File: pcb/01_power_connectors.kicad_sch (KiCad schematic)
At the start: 2 parts, among them J1 XT60PW-F, J2 XT60PW-M

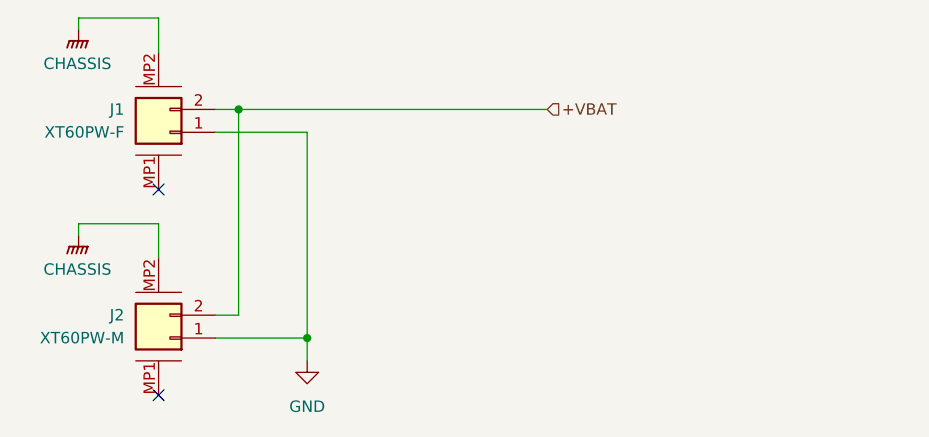
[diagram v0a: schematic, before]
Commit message: Added two XT-60 power connectors for daisy chaining multiple nodes together
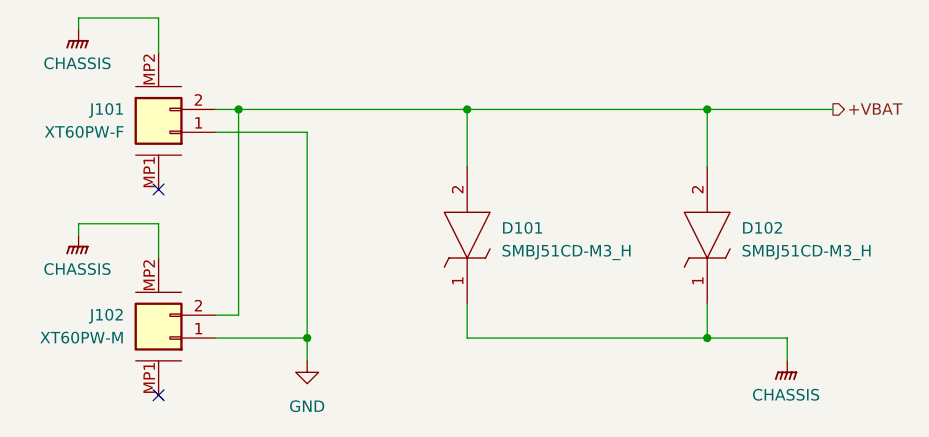
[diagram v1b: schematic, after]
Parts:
- added D101, D102: SMBJ51CD-M3_H, FluxNode-FOC:DIOM4336X24N, symbol FluxNode-FOC:SMBJ51CD-M3_H
- renumbered J1 to J101, J2 to J102
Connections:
- net +VBAT: now also D101.2, D102.2
- net CHASSIS: now also D101.1, D102.1

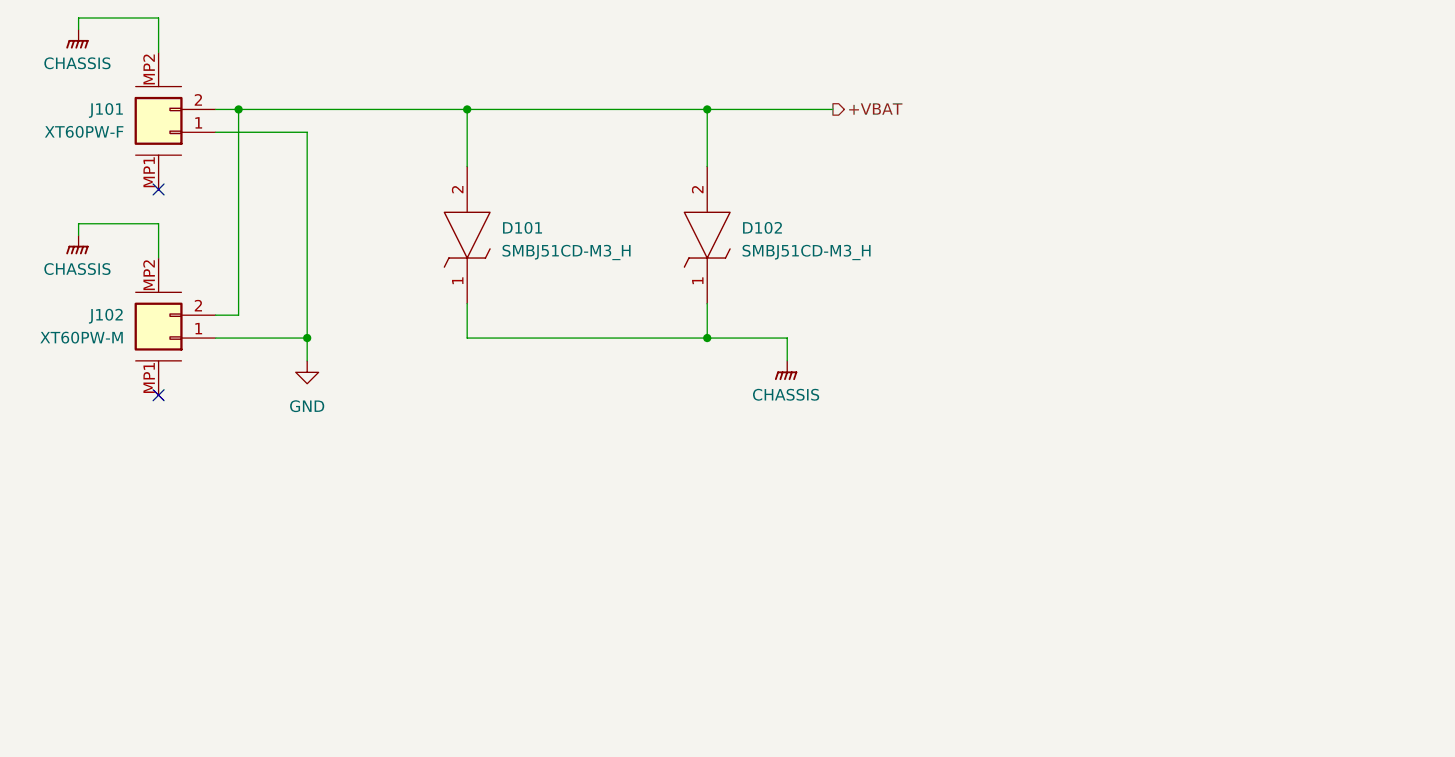
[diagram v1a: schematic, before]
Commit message: Unified all different LCSC part numbers of the same exact components to just one variant
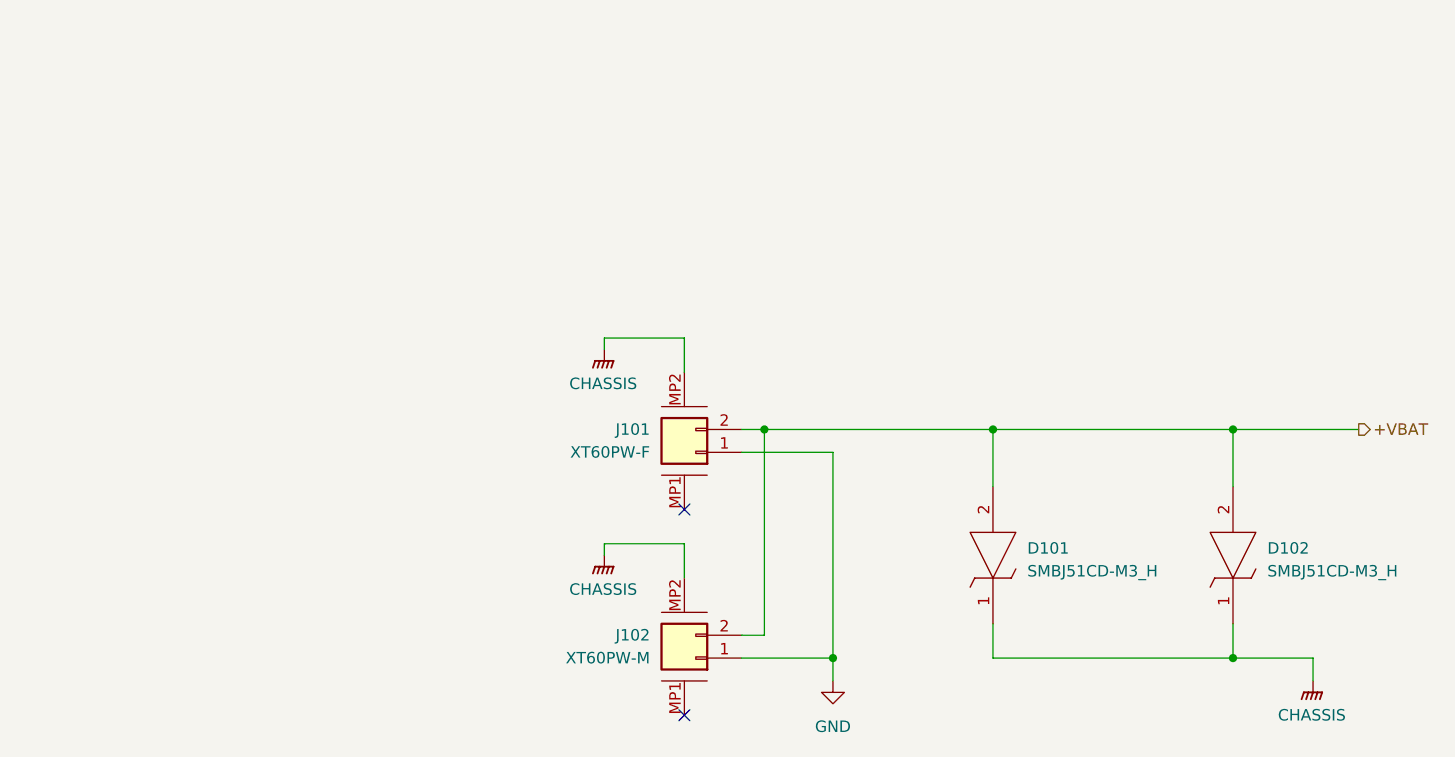
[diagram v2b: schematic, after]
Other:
- company: (none) -> PhiMai
- moved on the sheet: D101, D102, J101, J102

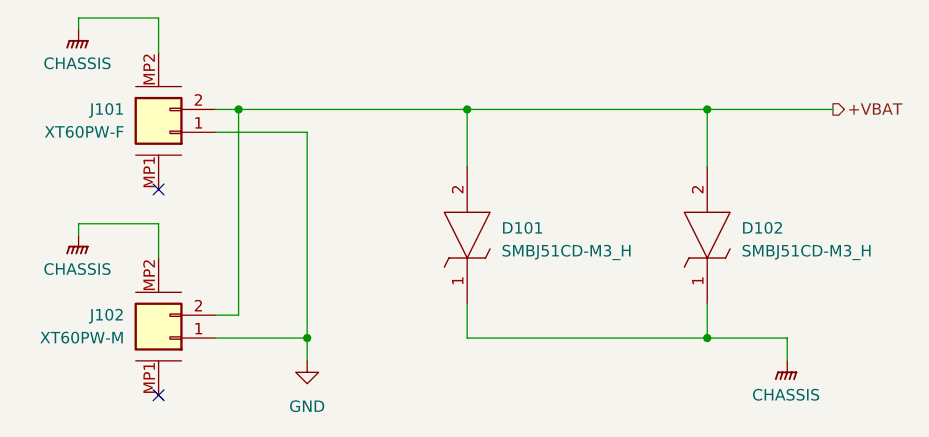
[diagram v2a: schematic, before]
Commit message: Some minor changes to the annotations
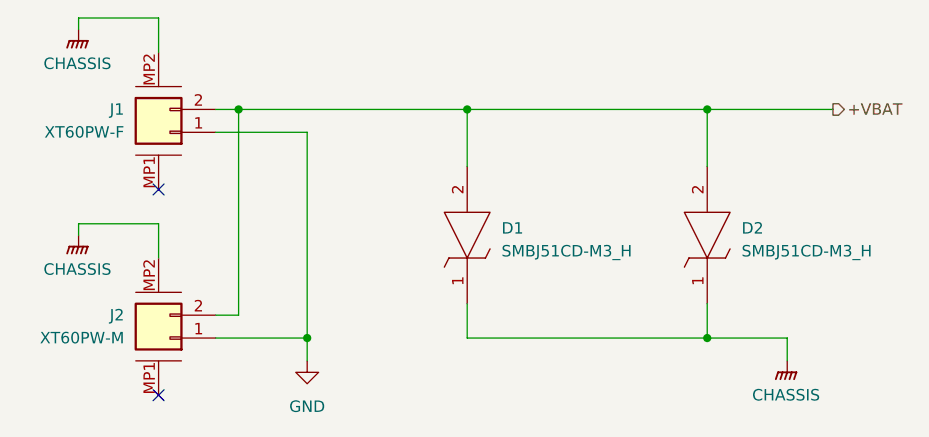
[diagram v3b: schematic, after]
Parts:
- renumbered D101 to D1, D102 to D2, J101 to J1, J102 to J2
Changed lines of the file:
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@@
 		(dnp no)
 		(fields_autoplaced yes)
-		(property "Reference" "#PWR0104"
+		(property "Reference" "#PWR09"
 			(at 179.07 107.95 0)
 			(hide yes)
@@
 			(project "FluxNode-FOC"
 				(path "/c3755418-04f3-4b36-86ed-bd05a53b8f5f/7c307646-0ecd-4068-a7a2-01ba516b03a7"
-					(reference "#PWR0104")
+					(reference "#PWR09")
 					(unit 1)
 				)
@@
 		(dnp no)
 		(fields_autoplaced yes)
-		(property "Reference" "#PWR0103"
+		(property "Reference" "#PWR08"
 			(at 125.73 109.22 0)
 			(hide yes)
@@
 			(project "FluxNode-FOC"
 				(path "/c3755418-04f3-4b36-86ed-bd05a53b8f5f/7c307646-0ecd-4068-a7a2-01ba516b03a7"
-					(reference "#PWR0103")
+					(reference "#PWR08")
 					(unit 1)
 				)
@@
 		(dnp no)
 		(fields_autoplaced yes)
-		(property "Reference" "J102"
+		(property "Reference" "J2"
 			(at 105.41 97.7899 0)
 			(show_name no)
@@
 			(project "FluxNode-FOC"
 				(path "/c3755418-04f3-4b36-86ed-bd05a53b8f5f/7c307646-0ecd-4068-a7a2-01ba516b03a7"
-					(reference "J102")
+					(reference "J2")
 					(unit 1)
 				)
@@
 		(dnp no)
 		(fields_autoplaced yes)
-		(property "Reference" "#PWR0101"
+		(property "Reference" "#PWR06"
 			(at 100.33 71.12 0)
 			(hide yes)
@@
 			(project "FluxNode-FOC"
 				(path "/c3755418-04f3-4b36-86ed-bd05a53b8f5f/7c307646-0ecd-4068-a7a2-01ba516b03a7"
-					(reference "#PWR0101")
+					(reference "#PWR06")
 					(unit 1)
 				)
@@
 		(dnp no)
 		(fields_autoplaced yes)
-		(property "Reference" "D102"
+		(property "Reference" "D2"
 			(at 173.99 88.1379 90)
 			(show_name no)
@@
 			(project "FluxNode-FOC"
 				(path "/c3755418-04f3-4b36-86ed-bd05a53b8f5f/7c307646-0ecd-4068-a7a2-01ba516b03a7"
-					(reference "D102")
+					(reference "D2")
 					(unit 1)
 				)
@@
 		(dnp no)
 		(fields_autoplaced yes)
-		(property "Reference" "#PWR0102"
+		(property "Reference" "#PWR07"
 			(at 100.33 93.98 0)
 			(hide yes)
@@
 			(project "FluxNode-FOC"
 				(path "/c3755418-04f3-4b36-86ed-bd05a53b8f5f/7c307646-0ecd-4068-a7a2-01ba516b03a7"
-					(reference "#PWR0102")
+					(reference "#PWR07")
 					(unit 1)
 				)
@@
 		(dnp no)
 		(fields_autoplaced yes)
-		(property "Reference" "D101"
+		(property "Reference" "D1"
 			(at 147.32 88.1379 90)
 			(show_name no)
@@
 			(project "FluxNode-FOC"
 				(path "/c3755418-04f3-4b36-86ed-bd05a53b8f5f/7c307646-0ecd-4068-a7a2-01ba516b03a7"
-					(reference "D101")
+					(reference "D1")
 					(unit 1)
 				)
@@
 		(dnp no)
 		(fields_autoplaced yes)
-		(property "Reference" "J101"
+		(property "Reference" "J1"
 			(at 105.41 74.9299 0)
 			(show_name no)
@@
 			(project "FluxNode-FOC"
 				(path "/c3755418-04f3-4b36-86ed-bd05a53b8f5f/7c307646-0ecd-4068-a7a2-01ba516b03a7"
-					(reference "J101")
+					(reference "J1")
 					(unit 1)
 				)
